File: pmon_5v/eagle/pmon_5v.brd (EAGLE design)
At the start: 60 x 60 mm, 33 parts, among them J1 USB, J2 USB, J3 USB_A, J4 PINHD-2X3, Q1 16Mhz, U1 LTC2943, U2 FT232RL, U3 ATMEGA328TQFP32, U4 TC1015

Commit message: Renamed +4V network to VCC. No semantic change.
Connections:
- net +4V renamed VCC
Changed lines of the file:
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@@
 <wire x1="47.9886" y1="22.098" x2="48.006" y2="22.098" width="0.4064" layer="1"/>
 </signal>
-<signal name="+4V">
+<signal name="VCC">
 <contactref element="R1" pad="2"/>
 <contactref element="R2" pad="2"/>

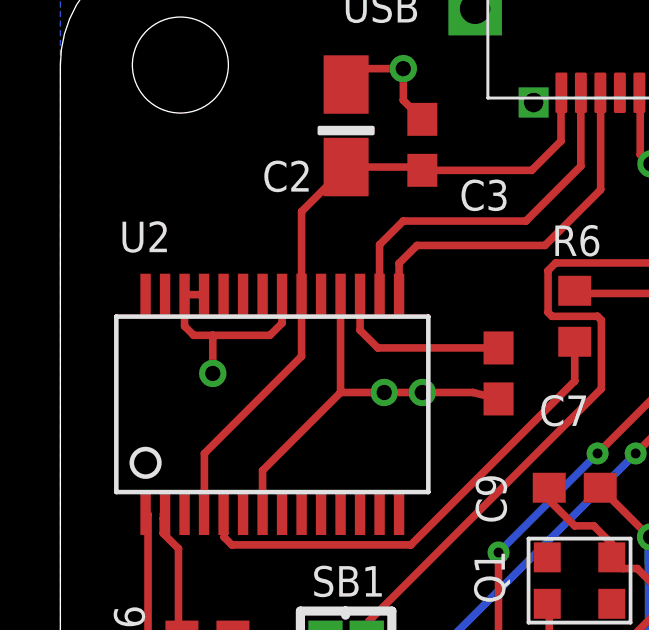
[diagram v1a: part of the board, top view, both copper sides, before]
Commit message: Minor layout change. Reroute a short between two pins to avoid reflow that looks like a solder bridge.
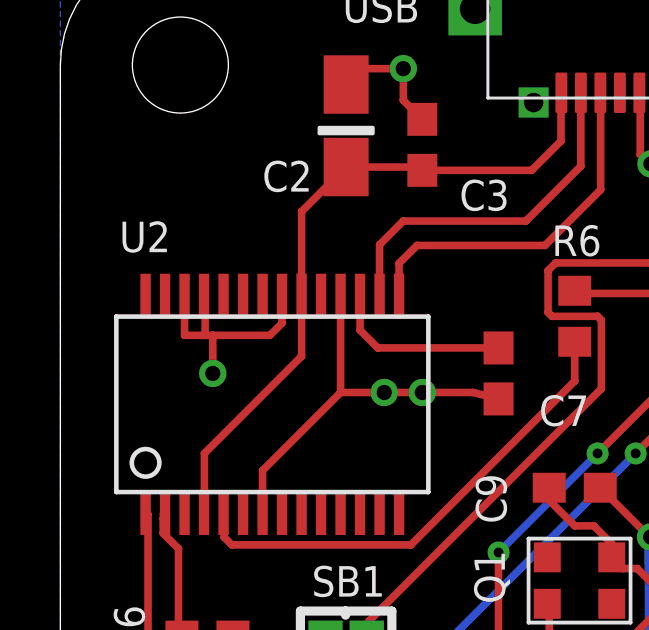
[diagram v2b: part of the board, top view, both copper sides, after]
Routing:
- net GND: track 82.9 -> 83.8 mm
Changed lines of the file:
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@@
 <via x="10.795" y="45.085" extent="1-16" drill="0.508"/>
 <via x="12.065" y="45.085" extent="1-16" drill="0.508"/>
-<wire x1="4.14" y1="48.346" x2="4.14" y2="47.295" width="0.254" layer="1"/>
-<wire x1="4.14" y1="47.295" x2="4.445" y2="46.99" width="0.254" layer="1"/>
-<wire x1="4.445" y1="46.99" x2="5.08" y2="46.99" width="0.254" layer="1"/>
+<wire x1="4.14" y1="48.346" x2="4.14" y2="46.99" width="0.254" layer="1"/>
+<wire x1="4.14" y1="46.99" x2="4.826" y2="46.99" width="0.254" layer="1"/>
+<wire x1="4.826" y1="46.99" x2="5.08" y2="46.99" width="0.254" layer="1"/>
 <wire x1="5.08" y1="46.99" x2="6.985" y2="46.99" width="0.254" layer="1"/>
 <wire x1="6.985" y1="46.99" x2="7.39" y2="47.395" width="0.254" layer="1"/>
 <wire x1="7.39" y1="47.395" x2="7.39" y2="48.346" width="0.254" layer="1"/>
-<wire x1="4.79" y1="48.346" x2="4.14" y2="48.346" width="0.254" layer="1"/>
 <wire x1="5.08" y1="46.99" x2="5.08" y2="45.72" width="0.254" layer="1"/>
 <via x="5.08" y="45.72" extent="1-16" drill="0.508"/>
@@
 <wire x1="30.06" y1="51.474" x2="30.06" y2="50.927" width="0.508" layer="1"/>
 <wire x1="29.679" y1="25.654" x2="31.623" y2="25.654" width="0.4064" layer="1"/>
+<wire x1="4.79" y1="48.346" x2="4.826" y2="48.346" width="0.254" layer="1"/>
+<wire x1="4.826" y1="48.346" x2="4.826" y2="46.99" width="0.254" layer="1"/>
 </signal>
 <signal name="+5V">
